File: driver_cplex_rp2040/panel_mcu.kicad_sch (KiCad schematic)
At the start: 23 parts, among them SW2 SW_Push, U5 RP2040, U6 W25Q128JVS, Y1 40MHz

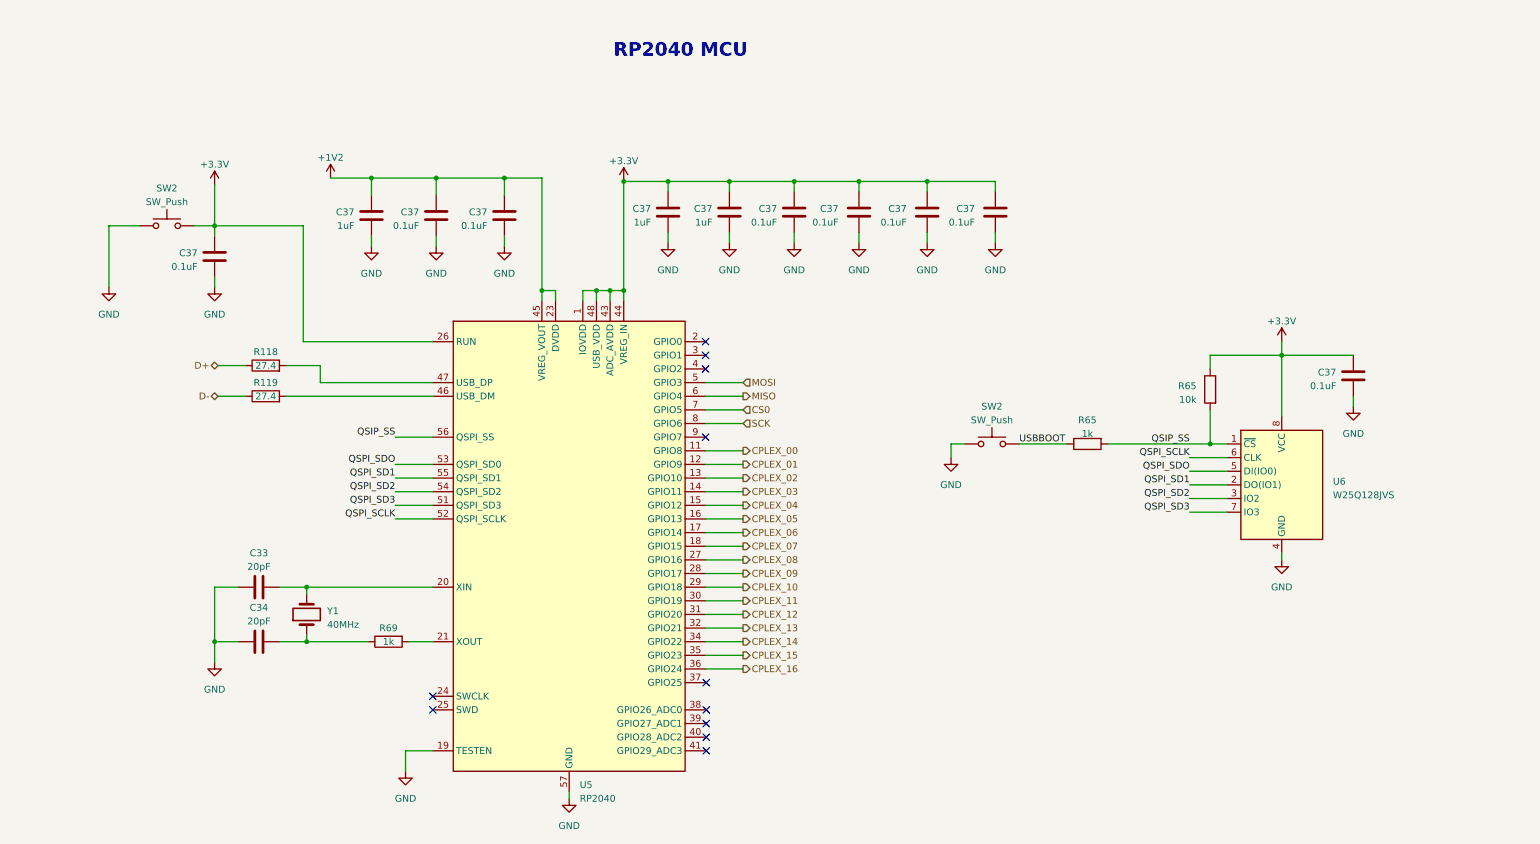
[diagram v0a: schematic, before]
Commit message: Added Charlieplexed version of rp2040 single pcb design.
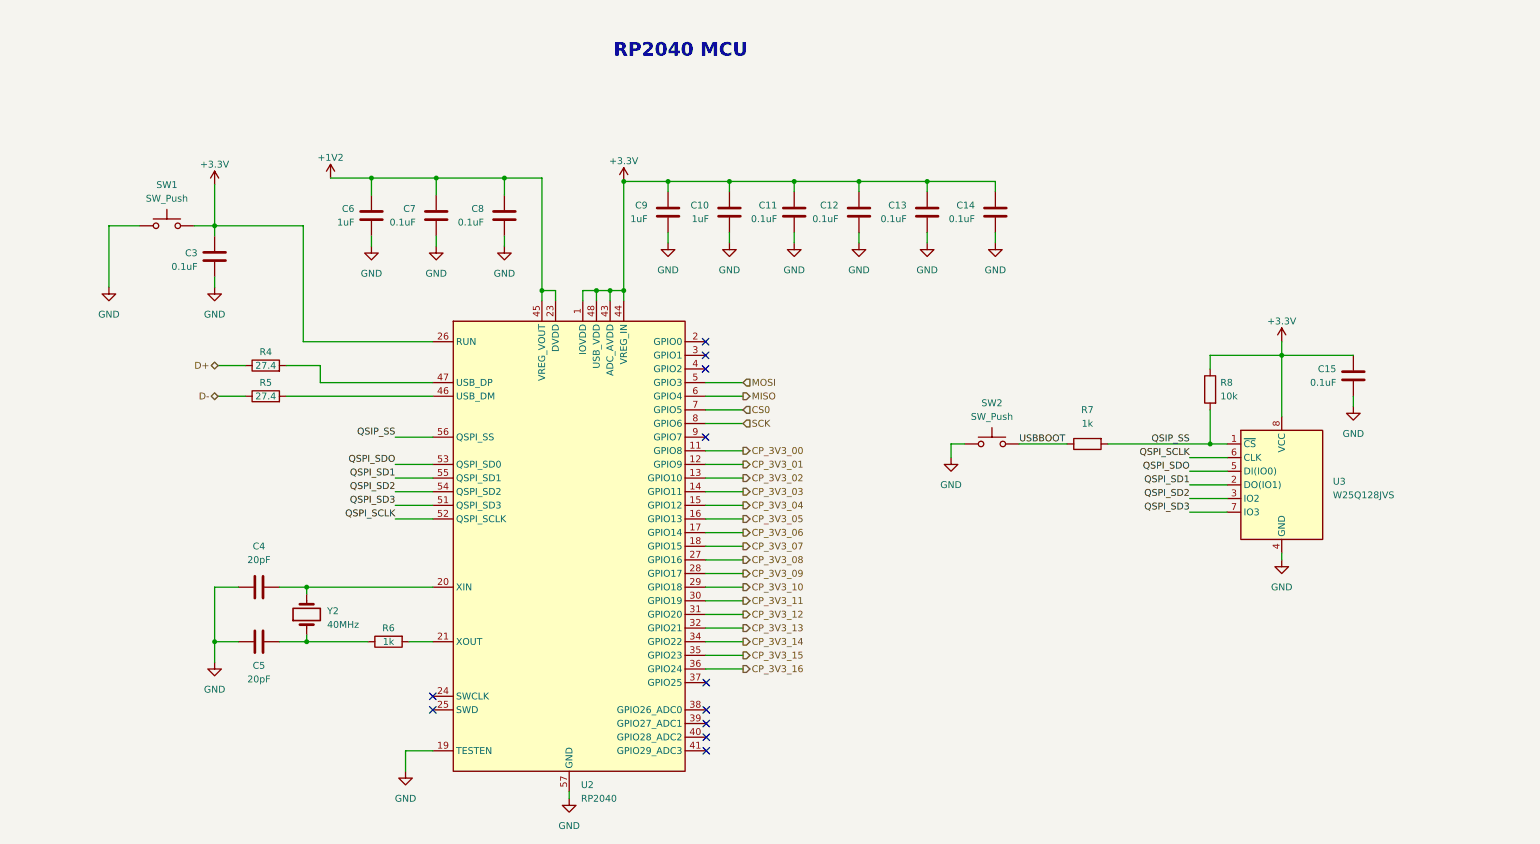
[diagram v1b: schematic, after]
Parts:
- renumbered C37 to C10, C37 to C11, C37 to C12, C37 to C13, C37 to C14, C37 to C15, C37 to C3, C33 to C4, C34 to C5, C37 to C6, C37 to C7, C37 to C8, C37 to C9, R118 to R4, R119 to R5, R69 to R6, R65 to R7, R65 to R8, SW2 to SW1, U5 to U2, U6 to U3, Y1 to Y2
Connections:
- net CPLEX_00 renamed CP_3V3_00
- net CPLEX_01 renamed CP_3V3_01
- net CPLEX_02 renamed CP_3V3_02
- net CPLEX_03 renamed CP_3V3_03
- net CPLEX_04 renamed CP_3V3_04
- net CPLEX_05 renamed CP_3V3_05
- net CPLEX_06 renamed CP_3V3_06
- net CPLEX_07 renamed CP_3V3_07
- net CPLEX_08 renamed CP_3V3_08
- net CPLEX_09 renamed CP_3V3_09
- net CPLEX_10 renamed CP_3V3_10
- net CPLEX_11 renamed CP_3V3_11
- net CPLEX_12 renamed CP_3V3_12
- net CPLEX_13 renamed CP_3V3_13
- net CPLEX_14 renamed CP_3V3_14
- net CPLEX_15 renamed CP_3V3_15
- net CPLEX_16 renamed CP_3V3_16

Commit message: Worked on footprint assignment for rp2040 single panel cplex design.
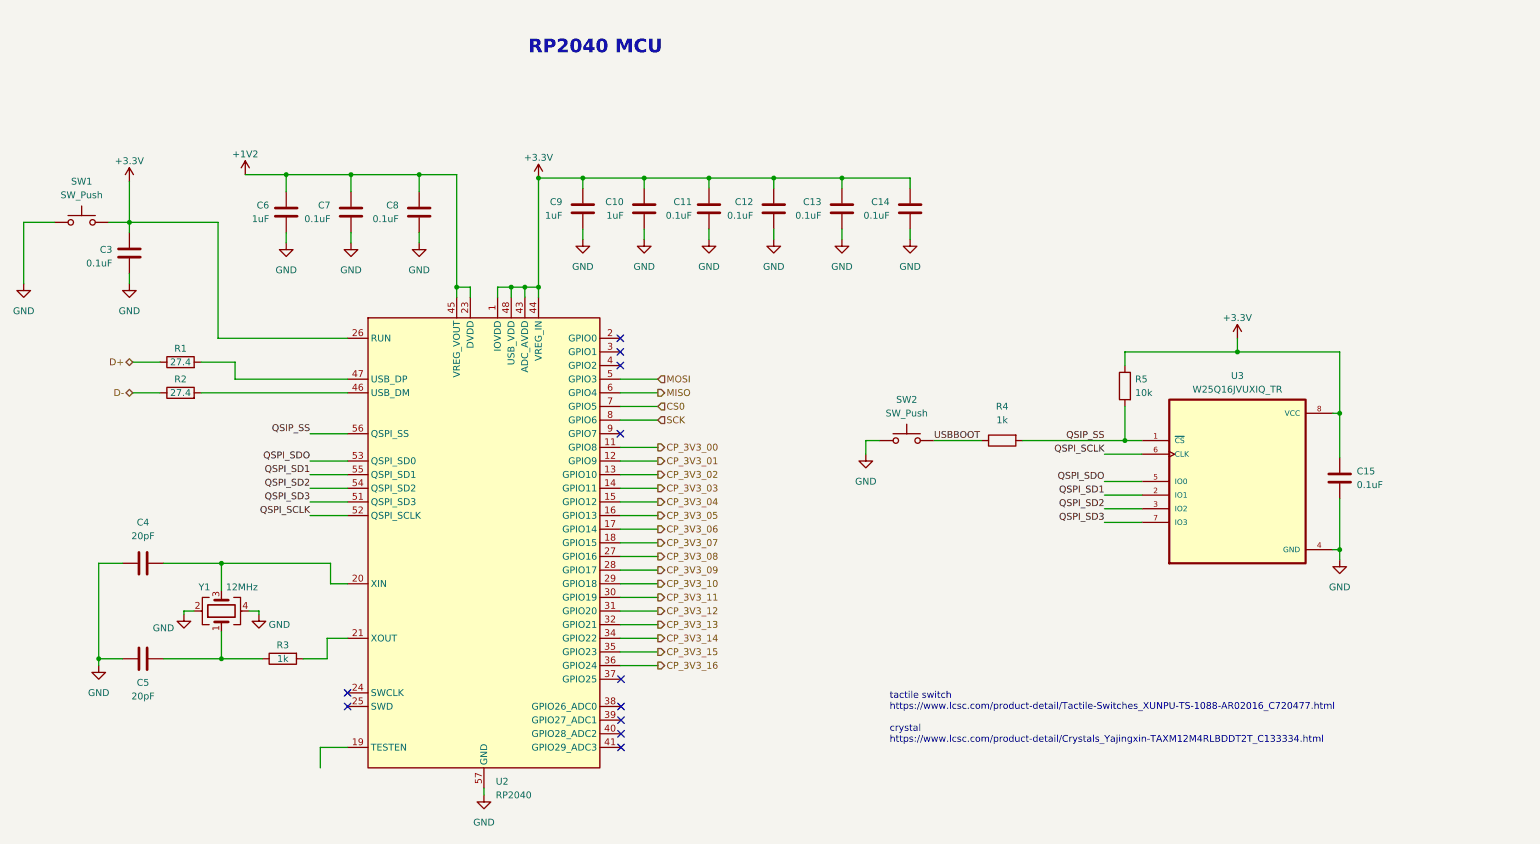
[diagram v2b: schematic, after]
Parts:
- removed U3: W25Q128JVS, Package_SO:SOIC-8_5.23x5.23mm_P1.27mm, symbol Memory_Flash:W25Q128JVS
- removed Y2: 40MHz, symbol Device:Crystal
- added U3: W25Q16JVUXIQ_TR, panel_custom:PSON50P300X200X60-9N, symbol panel_custom:W25Q16JVUXIQ_TR
- added Y1: 12MHz, panel_custom:Crystal_SMD_3225-4Pin_3.2x2.5mm, symbol Device:Crystal_GND24
- R1: renamed from R4; footprint (none) -> panel_custom:R_0201_0603Metric
- R2: renamed from R5; footprint (none) -> panel_custom:R_0201_0603Metric
- R3: renamed from R6; footprint (none) -> panel_custom:R_0201_0603Metric
- R4: renamed from R7; footprint (none) -> panel_custom:R_0201_0603Metric
- R5: renamed from R8; footprint (none) -> panel_custom:R_0201_0603Metric
- SW1, SW2: footprint (none) -> panel_custom:TS-1088-AR02016
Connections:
- net +3.3V: now also U3.8 (VCC)
- net GND: now also U3.4 (GND), Y1.2, Y1.4; no longer U2.19 (TESTEN)
- net QSIP_SS: now also U3.1 (~{CS})
- net QSPI_SCLK: now also U3.6 (CLK)
- net QSPI_SD1: now also U3.2 (IO1)
- net QSPI_SD2: now also U3.3 (IO2)
- net QSPI_SD3: now also U3.7 (IO3)
- net QSPI_SDO: now also U3.5 (IO0)
- net at C5.1, R3.1: now also Y1.1
- net at C4.1, U2.20 (XIN): now also Y1.3
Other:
- note added: "tactile switch https://www.lcsc.com/product-detail/Tactile-Switches_XUNPU-TS-1088-AR02016_C720477.html crystal https://www.lcsc.com/product-detail/Crystals_Yajingxin-TAXM12M4RLBDDT2T_C133334.html"
- moved on the sheet: C10, C11, C12, C13, C14, C15, C3, C4, C5, C6, C7, C8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

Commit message: Worked on layout.
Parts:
- U3: footprint panel_custom:PSON50P300X200X60-9N -> panel_custom:flashmem_PSON50P300X200X60-9N
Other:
- note added: "tactile switch https://www.lcsc.com/product-detail/Tactile-Switches_XUNPU-TS-1088-AR02016_C720477.html crystal https://www.lcsc.com/product-detail/Crystals_Yajingxin-TAXM12M4RLBDDT2T_C133334.html flash https://www.digikey.com/en/products/detail/winbond-electronics/W25Q16JVUXIQ-TR/15182017?s=N4IgTCBcDaIOpgKwEUCMA2AUgNQKoA0BJZEAXQF8g"
- note removed: "tactile switch https://www.lcsc.com/product-detail/Tactile-Switches_XUNPU-TS-1088-AR02016_C720477.html crystal https://www.lcsc.com/product-detail/Crystals_Yajingxin-TAXM12M4RLBDDT2T_C133334.html"
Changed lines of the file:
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@@
     (effects (font (size 2.54 2.54) (thickness 0.508) bold) (justify left bottom))
   )
-  (text "tactile switch\nhttps://www.lcsc.com/product-detail/Tactile-Switches_XUNPU-TS-1088-AR02016_C720477.html\n\ncrystal\nhttps://www.lcsc.com/product-detail/Crystals_Yajingxin-TAXM12M4RLBDDT2T_C133334.html"
-    (at 182.245 151.13 0)
-    (effects (font (size 1.27 1.27)) (justify left bottom))
+  (text "tactile switch\nhttps://www.lcsc.com/product-detail/Tactile-Switches_XUNPU-TS-1088-AR02016_C720477.html\n\ncrystal\nhttps://www.lcsc.com/product-detail/Crystals_Yajingxin-TAXM12M4RLBDDT2T_C133334.html\n\nflash\nhttps://www.digikey.com/en/products/detail/winbond-electronics/W25Q16JVUXIQ-TR/15182017?s=N4IgTCBcDaIOpgKwEUCMA2AUgNQKoA0BJZEAXQF8g"
+    (at 189.865 134.62 0)
+    (effects (font (size 0.762 0.762)) (justify left bottom))
   )
   (label "QSPI_SD2" (at 74.295 103.505 180) (fields_autoplaced)
@@
       (effects (font (size 1.27 1.27)))
     )
-    (property "Footprint" "panel_custom:PSON50P300X200X60-9N" (at 247.015 102.235 0)
+    (property "Footprint" "panel_custom:flashmem_PSON50P300X200X60-9N" (at 247.015 102.235 0)
       (effects (font (size 1.27 1.27)) (justify bottom) hide)
     )

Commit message: Worked on rp2040 cplex layout.
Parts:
- added C15, C16, C17, C18, C20: 0.1uF, panel_custom:C_0201_0603Metric, symbol Device:C
- renumbered C15 to C19
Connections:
- net +1V2: now also C20.2
- net +3.3V: now also C15.2, C16.2, C17.2, C18.2
- net GND: now also C15.1, C16.1, C17.1, C18.1, C20.1
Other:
- moved on the sheet: C10, C11, C12, C13, C14, C19, C3, C4, C5, C6, C7, C8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

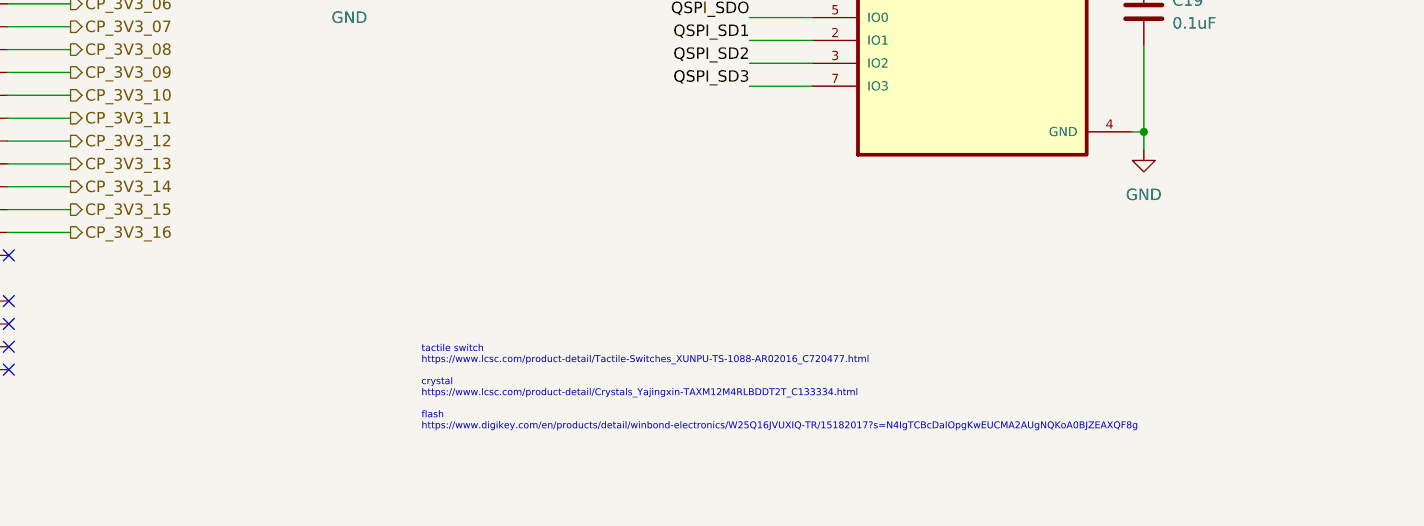
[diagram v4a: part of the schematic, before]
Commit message: Work on rp2040 cplex'd design routing and layout.
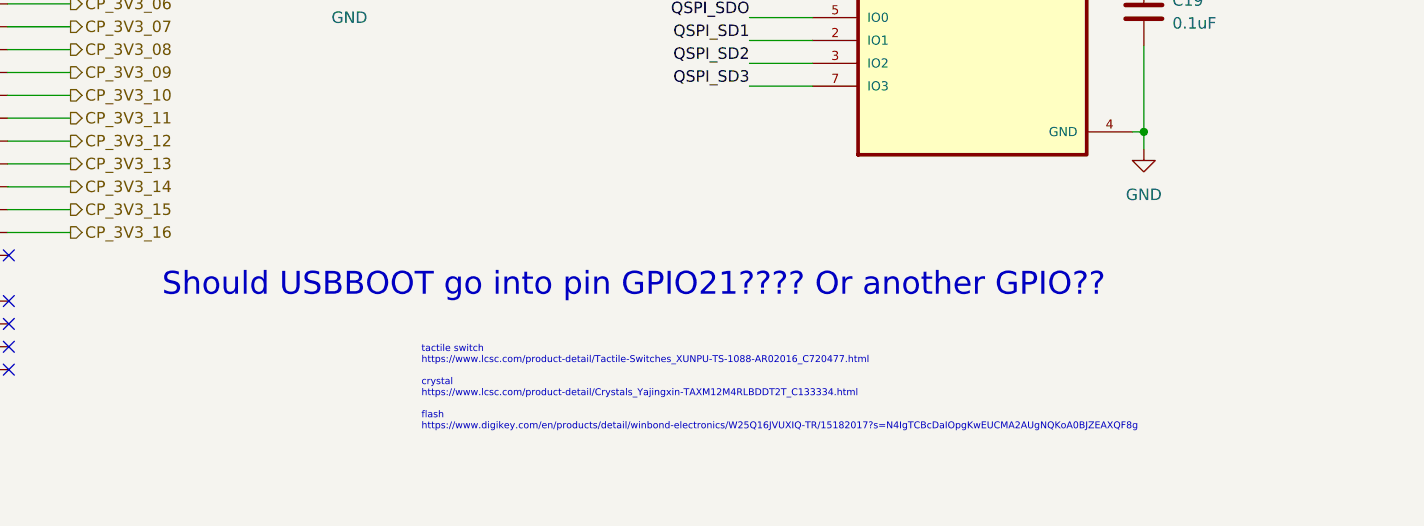
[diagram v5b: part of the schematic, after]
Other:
- note added: "Should USBBOOT go into pin GPIO21???? Or another GPIO??"
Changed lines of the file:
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@@
     (effects (font (size 0.762 0.762)) (justify left bottom))
+  )
+  (text "Should USBBOOT go into pin GPIO21???? Or another GPIO??"
+    (at 163.195 139.954 0)
+    (effects (font (size 2.54 2.54)) (justify left bottom))
   )
   (label "QSPI_SD2" (at 88.265 99.568 180) (fields_autoplaced)

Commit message: Worked on production files.
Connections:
- net GND: now also U2.19 (TESTEN)
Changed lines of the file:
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@@
   (junction (at 253.238 84.582) (diameter 0) (color 0 0 0 0)
   )
-  (no_connect (at 146.177 147.828))
-  (no_connect (at 146.177 142.748))
+  (no_connect (at 146.05 135.128))
   (no_connect (at 95.25 140.208))
-  (no_connect (at 146.177 145.288))
   (no_connect (at 146.05 76.708))
   (no_connect (at 146.05 71.628))
-  (no_connect (at 146.177 135.128))
   (no_connect (at 146.05 74.168))
   (no_connect (at 146.05 89.408))
-  (no_connect (at 146.177 140.208))
+  (no_connect (at 146.05 140.208))
+  (no_connect (at 146.05 147.828))
   (no_connect (at 95.25 137.668))
+  (no_connect (at 146.05 145.288))
+  (no_connect (at 146.05 142.748))
   (wire (pts (xy 139.065 41.783) (xy 150.495 41.783))
     (stroke (width 0) (type default))
@@
         )
       )
+    )
+  )
+  (symbol (lib_id "power:GND") (at 90.17 151.638 0) (mirror y) (unit 1)
+    (in_bom yes) (on_board yes) (dnp no) (fields_autoplaced)
+    (property "Reference" "#PWR062" (at 90.17 157.988 0)
+      (effects (font (size 1.27 1.27)) hide)
+    )
+    (property "Value" "GND" (at 90.17 156.718 0)
+      (effects (font (size 1.27 1.27)))
+    )
+    (property "Footprint" "" (at 90.17 151.638 0)
+      (effects (font (size 1.27 1.27)) hide)
+    )
+    (property "Datasheet" "" (at 90.17 151.638 0)
+      (effects (font (size 1.27 1.27)) hide)
+    )
+    (pin "1")
+    (instances
+      (project "driver_cplex_rp2040"
+        (path "/1e634561-32a0-4ffa-9d4f-e93f355464d5/b30b56c6-21ca-46ed-bb1a-e5062fd43ea8"
+          (reference "#PWR062") (unit 1)
+        )
+      )
